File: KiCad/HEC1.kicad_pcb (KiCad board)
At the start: 2 copper layers, 243.8 x 170.2 mm, 36 parts, among them J1 Barrel_Jack_Switch, U1 Z80CPU, U10 74LS30, U11 74LS10, U11 74LS32, U12 74LS04, U13 74LS245, U14 74LS245, U15 74LS32, U16 74LS32, U17 74LS30, U17 74LS74, U18 74LS02, U18 74LS74, U19 74LS30, U2 AS6C4008-55PCN, U20 74LS574, U21 74LS574, U22 74LS02, U23 74LS74, U24 74LS74, U25 74LS541, U26 74LS541, U27 74LS74, U3 AS6C4008-55PCN, U4 CY7C199, U5 CY7C199, U6 74LS138, U7 28C256, U8 74LS138, U9 74LS574

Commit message: Add HEC Bus
The HEC bus packs a lot of information into a small amount of pins. It is suitable for cards with various complexity.
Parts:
- added REF**: edge_connector_8pin, Library:edge_connector_8pin, F.Cu at (66.0, 45.7)
- added REF**: edge_connector_36pin, Library:edge_connector_36pin, F.Cu at (66.0, 81.3)
- added REF**: edge_connector_8pin, Library:edge_connector_8pin, F.Cu at (124.5, 45.7)
- added REF**: edge_connector_36pin, Library:edge_connector_36pin, F.Cu at (154.9, 81.3)
- added REF**: edge_connector_36pin, Library:edge_connector_36pin, F.Cu at (96.5, 81.3)
- added REF**: edge_connector_8pin, Library:edge_connector_8pin, F.Cu at (96.5, 45.7)
- added REF**: edge_connector_8pin, Library:edge_connector_8pin, F.Cu at (154.9, 45.7)
- added REF**: edge_connector_36pin, Library:edge_connector_36pin, F.Cu at (124.5, 81.3)
- moved U11 317.2 mm to (428.9, 50.8)
- moved U11 317.2 mm to (413.7, -2.54)
- moved U12 317.2 mm to (440.7, 50.8)
- moved U15 317.2 mm to (368.3, 22.9)
- moved U16 317.2 mm to (380.1, 22.9)
- moved U20 317.2 mm to (403.4, 50.8)
- moved U21 317.2 mm to (415.2, 50.8)
- moved U22 317.2 mm to (425.4, -2.54)
- moved U6 317.2 mm to (413.7, 17.0)
- moved U6 317.2 mm to (428.9, 72.3)
- moved U7 317.2 mm to (384.0, 50.8)
- moved U8 317.2 mm to (425.4, 17.0)
- moved U9 317.2 mm to (393.4, 17.9)
- moved U10 283.6 mm to (325.1, 78.7)
- moved U1 188.0 mm to (332.7, 127.0)
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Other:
- outline, holes or cut-outs redrawn

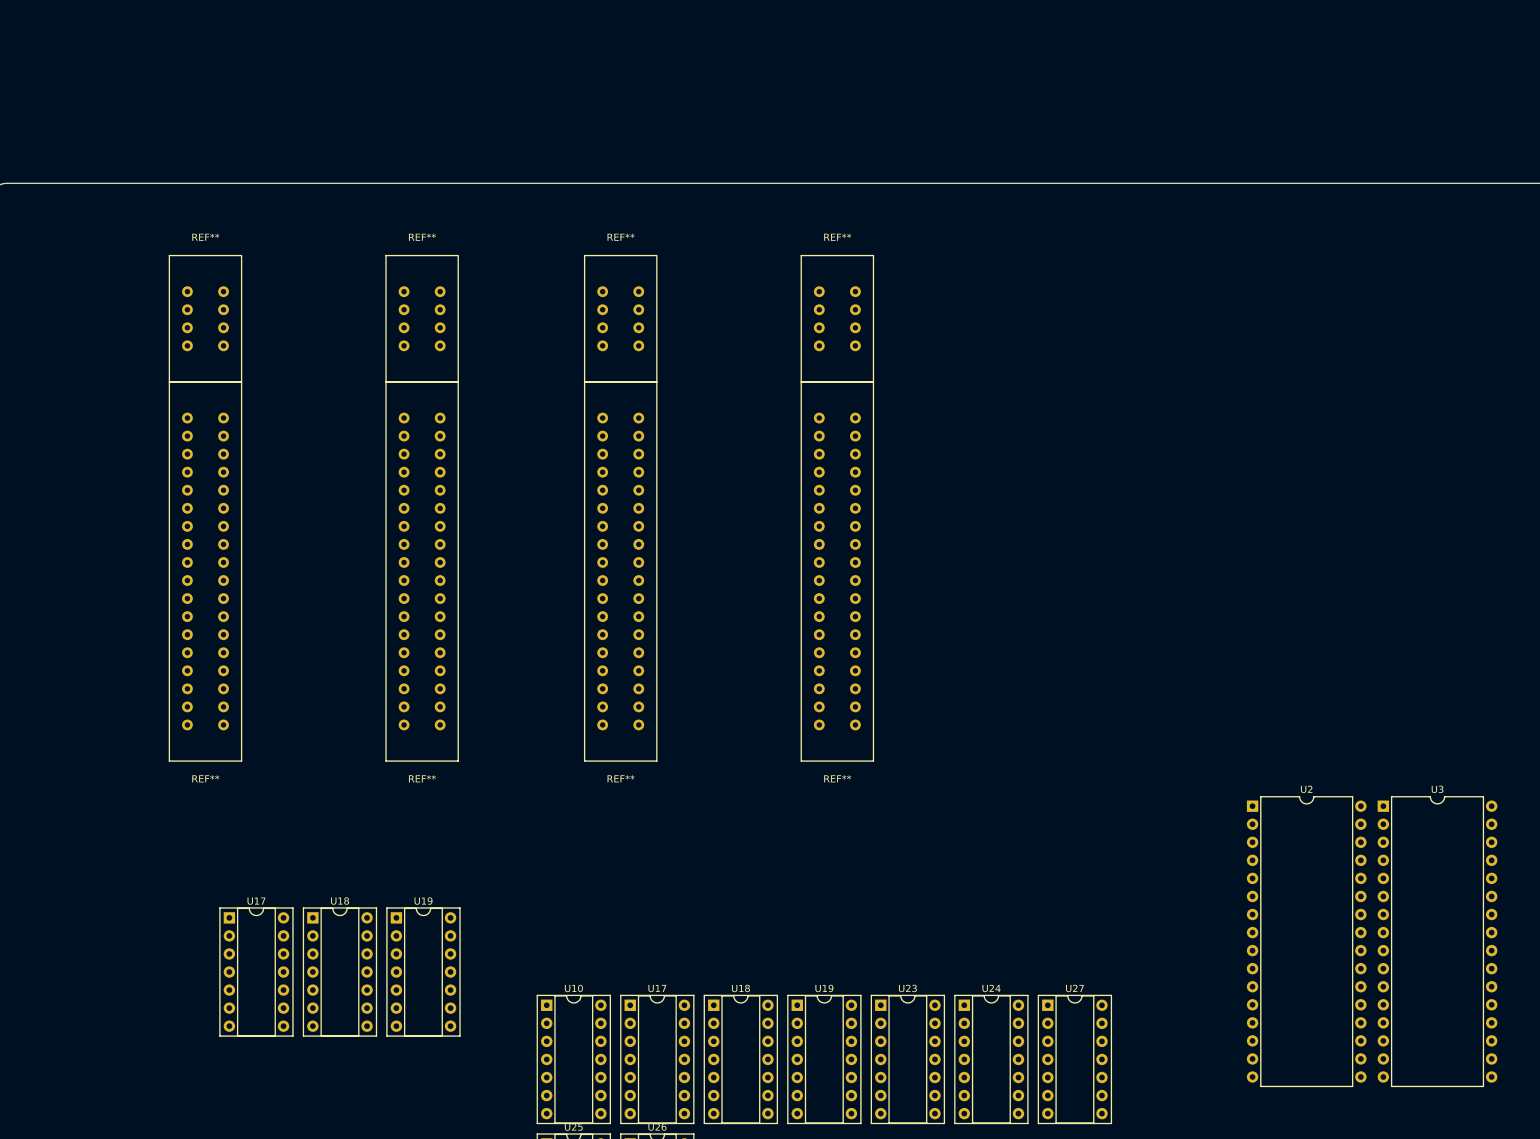
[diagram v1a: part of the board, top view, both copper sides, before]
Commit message: Created footprint for HEC bus
Created footprints for HEC bus and some other updates.
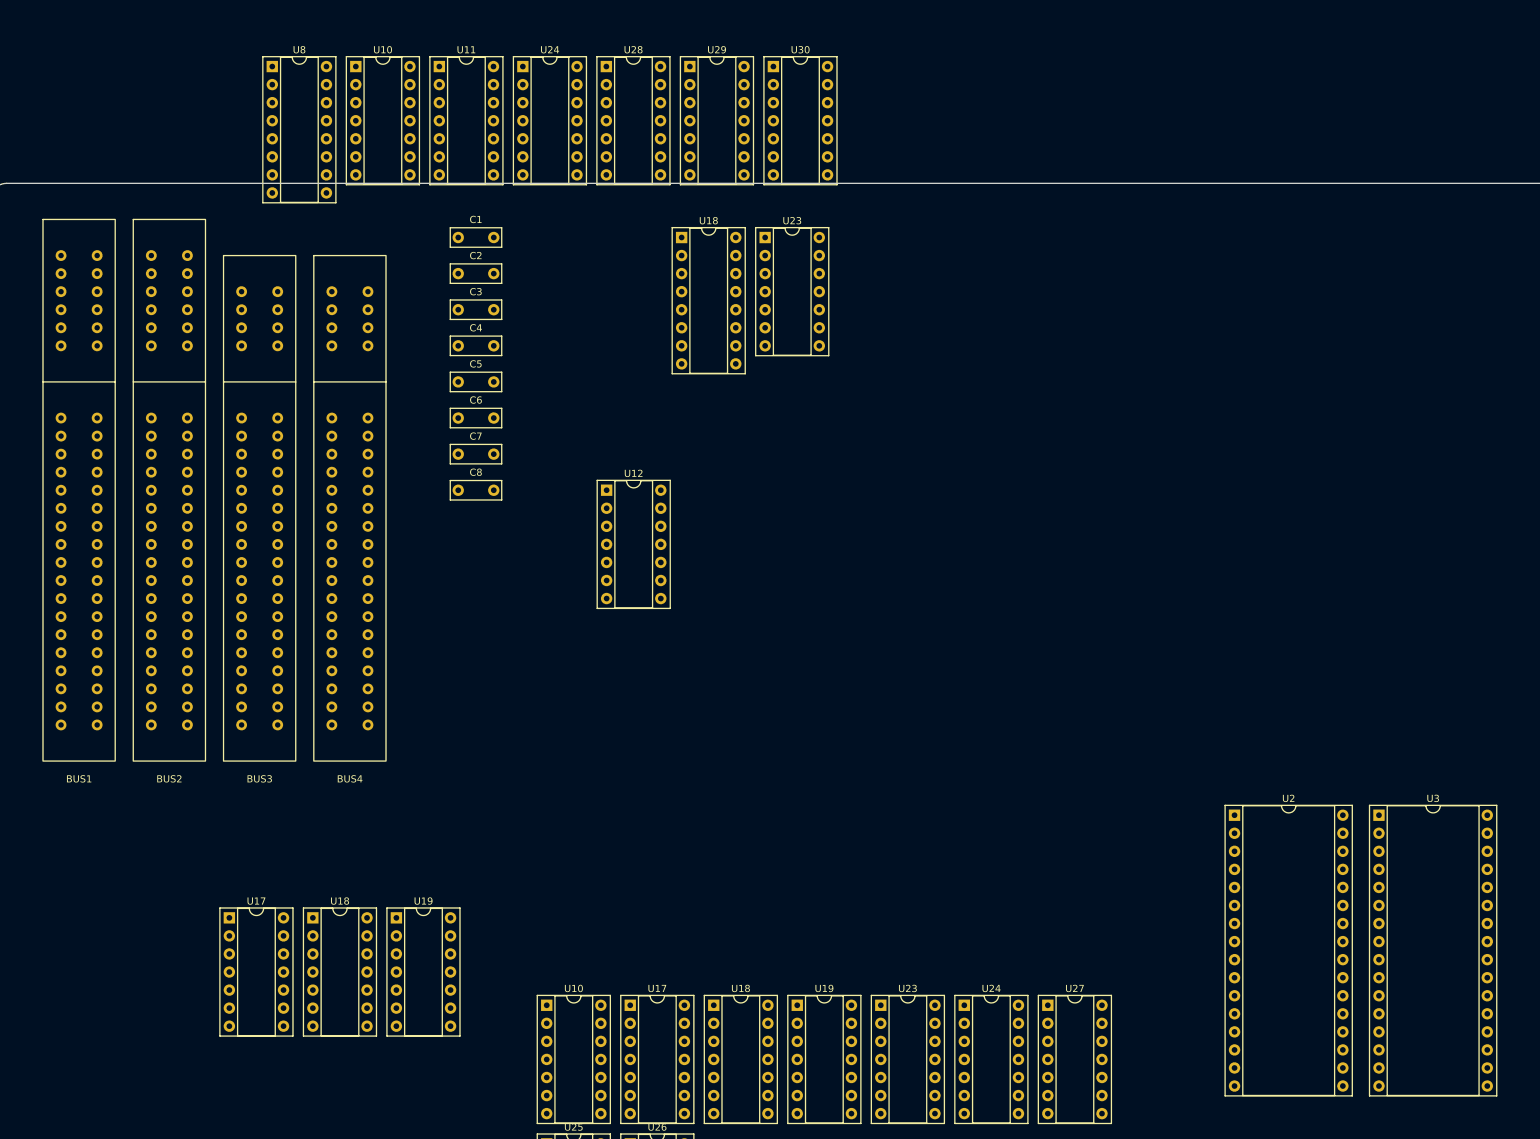
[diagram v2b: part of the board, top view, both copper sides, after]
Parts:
- removed REF** (x4): edge_connector_8pin, Library:edge_connector_8pin
- removed REF** (x4): edge_connector_36pin, Library:edge_connector_36pin
- added BUS1: ~, Library:Bus_HEC, F.Cu at (48.3, 68.6)
- added BUS2: ~, Library:Bus_HEC, F.Cu at (61.0, 68.6)
- added BUS3: ~, Library:Bus_HEC_5Vonly, F.Cu at (73.7, 68.6)
- added BUS4: ~, Library:Bus_HEC_5Vonly, F.Cu at (86.4, 68.6)
- added C1: C, Capacitor_THT:C_Disc_D7.0mm_W2.5mm_P5.00mm, F.Cu at (101.6, 33.0)
- added C2: C, Capacitor_THT:C_Disc_D7.0mm_W2.5mm_P5.00mm, F.Cu at (101.6, 38.1)
- added C3: C, Capacitor_THT:C_Disc_D7.0mm_W2.5mm_P5.00mm, F.Cu at (101.6, 43.2)
- added C4: C, Capacitor_THT:C_Disc_D7.0mm_W2.5mm_P5.00mm, F.Cu at (101.6, 48.3)
- added C5: C, Capacitor_THT:C_Disc_D7.0mm_W2.5mm_P5.00mm, F.Cu at (101.6, 53.3)
- added C6: C, Capacitor_THT:C_Disc_D7.0mm_W2.5mm_P5.00mm, F.Cu at (101.6, 58.4)
- added C7: C, Capacitor_THT:C_Disc_D7.0mm_W2.5mm_P5.00mm, F.Cu at (101.6, 63.5)
- added C8: C, Capacitor_THT:C_Disc_D7.0mm_W2.5mm_P5.00mm, F.Cu at (101.6, 68.6)
- added U10: 74LS32, Package_DIP:DIP-14_W7.62mm_Socket, F.Cu at (87.2, 8.97)
- added U11: 74LS00, Package_DIP:DIP-14_W7.62mm_Socket, F.Cu at (98.9, 8.97)
- added U12: 74LS04, Package_DIP:DIP-14_W7.62mm_Socket, F.Cu at (122.5, 68.6)
- added U18: 74LS138, Package_DIP:DIP-16_W7.62mm_Socket, F.Cu at (133.0, 33.0)
- added U23: 74LS74, Package_DIP:DIP-14_W7.62mm_Socket, F.Cu at (144.8, 33.0)
- added U24: 74LS74, Package_DIP:DIP-14_W7.62mm_Socket, F.Cu at (110.7, 8.97)
- added U28: 74LS20, Package_DIP:DIP-14_W7.62mm_Socket, F.Cu at (122.4, 8.97)
- added U29: 74LS74, Package_DIP:DIP-14_W7.62mm_Socket, F.Cu at (134.2, 8.97)
- added U30: 74LS74, Package_DIP:DIP-14_W7.62mm_Socket, F.Cu at (145.9, 8.97)
- added U8: 74LS138, Package_DIP:DIP-16_W7.62mm_Socket, F.Cu at (75.4, 8.97)
- U2, U3: footprint Package_DIP:DIP-32_W15.24mm -> Package_DIP:DIP-32_W15.24mm_Socket
- moved U2 2.84 mm to (210.8, 114.3)
- moved U3 1.41 mm to (231.1, 114.3)
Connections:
- J1 pad 1: unconnected-(J1-Pad1) -> VCC
- J1 pad 2: Net-(J1-Pad2) -> GND
- J1 pad 3: Net-(J1-Pad2) -> GND
- RN1 pad 1: /MEC_Protection/H -> H
- U1 pad 1: /HEC_CPU/A11 -> /HEC_Memory/A11
- U1 pad 10: /HEC_CPU/D6 -> /HEC_Memory/D6
- U1 pad 12: /HEC_CPU/D2 -> /HEC_Memory/D2
- U1 pad 13: /HEC_CPU/D7 -> /HEC_Memory/D7
- U1 pad 14: /HEC_CPU/D0 -> /HEC_Memory/D0
- U1 pad 15: /HEC_CPU/D1 -> /HEC_Memory/D1
- U1 pad 2: /HEC_CPU/A12 -> /HEC_Memory/A12
- U1 pad 3: /HEC_CPU/A13 -> /HEC_Memory/A13
- U1 pad 30: /HEC_CPU/A0 -> /HEC_Memory/A0
- U1 pad 31: /HEC_CPU/A1 -> /HEC_Memory/A1
- U1 pad 32: /HEC_CPU/A2 -> /HEC_Memory/A2
- U1 pad 33: /HEC_CPU/A3 -> /HEC_Memory/A3
- U1 pad 34: /HEC_CPU/A4 -> /HEC_Memory/A4
- U1 pad 35: /HEC_CPU/A5 -> /HEC_Memory/A5
- U1 pad 36: /HEC_CPU/A6 -> /HEC_Memory/A6
- U1 pad 37: /HEC_CPU/A7 -> /HEC_Memory/A7
- U1 pad 38: /HEC_CPU/A8 -> /HEC_Memory/A8
- U1 pad 39: /HEC_CPU/A9 -> /HEC_Memory/A9
- U1 pad 4: /HEC_CPU/A14 -> /HEC_Memory/A14
- U1 pad 40: /HEC_CPU/A10 -> /HEC_Memory/A10
- U1 pad 5: /HEC_CPU/A15 -> /HEC_Memory/A15
- U1 pad 7: /HEC_CPU/D4 -> /HEC_Memory/D4
- U1 pad 8: /HEC_CPU/D3 -> /HEC_Memory/D3
- U1 pad 9: /HEC_CPU/D5 -> /HEC_Memory/D5
- U17 pad 14: unconnected-(U17B-VCC-Pad14) -> VCC
- U17 pad 7: unconnected-(U17B-GND-Pad7) -> GND
- U17 pad 8: Net-(U17-Pad8) -> Net-(U10-Pad12)
- U19 pad 1: /MEC_Protection/D0 -> /HEC_Memory/A0
- U19 pad 11: /MEC_Protection/H -> H
- U19 pad 12: /MEC_Protection/H -> H
- U19 pad 2: /MEC_Protection/D1 -> /HEC_Memory/A1
- U19 pad 3: /MEC_Protection/D2 -> /HEC_Memory/A2
- U19 pad 4: /MEC_Protection/D6 -> /HEC_Memory/A6
- U19 pad 5: /MEC_Protection/D7 -> /HEC_Memory/A7
- U20 pad 12: /HEC_CPU/D7 -> /HEC_Memory/D7
- U20 pad 13: /HEC_CPU/D6 -> /HEC_Memory/D6
- U20 pad 14: /HEC_CPU/D5 -> /HEC_Memory/D5
- U20 pad 15: /HEC_CPU/D4 -> /HEC_Memory/D4
- U20 pad 16: /HEC_CPU/D3 -> /HEC_Memory/D3
- U20 pad 17: /HEC_CPU/D2 -> /HEC_Memory/D2
- U20 pad 18: /HEC_CPU/D1 -> /HEC_Memory/D1
- U20 pad 19: /HEC_CPU/D0 -> /HEC_Memory/D0
- U20 pad 2: /HEC_CPU/A0 -> /HEC_Memory/A0
- U20 pad 3: /HEC_CPU/A1 -> /HEC_Memory/A1
- U20 pad 4: /HEC_CPU/A2 -> /HEC_Memory/A2
- U20 pad 5: /HEC_CPU/A3 -> /HEC_Memory/A3
- U20 pad 6: /HEC_CPU/A4 -> /HEC_Memory/A4
- U20 pad 7: /HEC_CPU/A5 -> /HEC_Memory/A5
- U20 pad 8: /HEC_CPU/A6 -> /HEC_Memory/A6
- U20 pad 9: /HEC_CPU/A7 -> /HEC_Memory/A7
- U21 pad 12: /HEC_CPU/D7 -> /HEC_Memory/D7
- U21 pad 13: /HEC_CPU/D6 -> /HEC_Memory/D6
- U21 pad 14: /HEC_CPU/D5 -> /HEC_Memory/D5
- U21 pad 15: /HEC_CPU/D4 -> /HEC_Memory/D4
- U21 pad 16: /HEC_CPU/D3 -> /HEC_Memory/D3
- U21 pad 17: /HEC_CPU/D2 -> /HEC_Memory/D2
- U21 pad 18: /HEC_CPU/D1 -> /HEC_Memory/D1
- U21 pad 19: /HEC_CPU/D0 -> /HEC_Memory/D0
- U21 pad 2: /HEC_CPU/A8 -> /HEC_Memory/A8
- U21 pad 3: /HEC_CPU/A9 -> /HEC_Memory/A9
- U21 pad 4: /HEC_CPU/A10 -> /HEC_Memory/A10
- U21 pad 5: /HEC_CPU/A11 -> /HEC_Memory/A11
- U21 pad 6: /HEC_CPU/A12 -> /HEC_Memory/A12
- U21 pad 7: /HEC_CPU/A13 -> /HEC_Memory/A13
- U21 pad 8: /HEC_CPU/A14 -> /HEC_Memory/A14
- U21 pad 9: /HEC_CPU/A15 -> /HEC_Memory/A15
- U22 pad 1: (no net) -> unconnected-(U22-Pad1)
- U22 pad 11: unconnected-(U22-Pad11) -> /MEC_Protection/SYS
- U22 pad 12: unconnected-(U22-Pad12) -> /MEC_Protection/~{IORQ}
- U22 pad 13: unconnected-(U22-Pad13) -> Net-(U30A-C)
- U22 pad 2: (no net) -> unconnected-(U22-Pad2)
- U22 pad 3: (no net) -> unconnected-(U22-Pad3)
- U25 pad 1: unconnected-(U25-G1-Pad1) -> /HEC_CPU/~{RD}
- U25 pad 10: unconnected-(U25-GND-Pad10) -> GND
- U25 pad 11: unconnected-(U25-Y7-Pad11) -> /HEC_Memory/A7
- U25 pad 12: unconnected-(U25-Y6-Pad12) -> /HEC_Memory/A6
- U25 pad 13: unconnected-(U25-Y5-Pad13) -> /HEC_Memory/A5
- U25 pad 14: unconnected-(U25-Y4-Pad14) -> /HEC_Memory/A4
- U25 pad 15: unconnected-(U25-Y3-Pad15) -> /HEC_Memory/A3
- U25 pad 16: unconnected-(U25-Y2-Pad16) -> /HEC_Memory/A2
- U25 pad 17: unconnected-(U25-Y1-Pad17) -> /HEC_Memory/A1
- U25 pad 18: unconnected-(U25-Y0-Pad18) -> /HEC_Memory/A0
- U25 pad 19: unconnected-(U25-G2-Pad19) -> /MEC_Protection/~{INT_SOURCE_1}
- U25 pad 20: unconnected-(U25-VCC-Pad20) -> VCC
- U26 pad 1: unconnected-(U26-G1-Pad1) -> /HEC_CPU/~{RD}
- U26 pad 10: unconnected-(U26-GND-Pad10) -> GND
- U26 pad 11: unconnected-(U26-Y7-Pad11) -> /HEC_Memory/A7
- U26 pad 12: unconnected-(U26-Y6-Pad12) -> /HEC_Memory/A6
- U26 pad 13: unconnected-(U26-Y5-Pad13) -> /HEC_Memory/A5
- U26 pad 14: unconnected-(U26-Y4-Pad14) -> /HEC_Memory/A4
- U26 pad 15: unconnected-(U26-Y3-Pad15) -> /HEC_Memory/A3
- U26 pad 16: unconnected-(U26-Y2-Pad16) -> /HEC_Memory/A2
- U26 pad 17: unconnected-(U26-Y1-Pad17) -> /HEC_Memory/A1
- U26 pad 18: unconnected-(U26-Y0-Pad18) -> /HEC_Memory/A0
- U26 pad 19: unconnected-(U26-G2-Pad19) -> /MEC_Protection/~{INT_SOURCE_2}
- U26 pad 2: /MEC_Protection/lastsys -> /MEC_Protection/~{EXT_INT0}
- U26 pad 20: unconnected-(U26-VCC-Pad20) -> VCC
- U27 pad 1: Net-(U23B-Q) -> /HEC_CPU/~{NMI}
- U27 pad 10: /MEC_Protection/H -> H
- U27 pad 13: /MEC_Protection/H -> H
- U6 pad 1: /HEC_CPU/A4 -> /HEC_Memory/A4
- U6 pad 2: /HEC_CPU/A5 -> /HEC_Memory/A5
- U6 pad 3: /HEC_CPU/A6 -> /HEC_Memory/A6
- U6 pad 4: /HEC_CPU/A7 -> /HEC_Memory/A7
- U7 pad 1: /HEC_CPU/A14 -> /HEC_Memory/A14
- U7 pad 10: /HEC_CPU/A0 -> /HEC_Memory/A0
- U7 pad 11: /HEC_CPU/D0 -> /HEC_Memory/D0
- U7 pad 12: /HEC_CPU/D1 -> /HEC_Memory/D1
- U7 pad 13: /HEC_CPU/D2 -> /HEC_Memory/D2
- U7 pad 15: /HEC_CPU/D3 -> /HEC_Memory/D3
- U7 pad 16: /HEC_CPU/D4 -> /HEC_Memory/D4
- U7 pad 17: /HEC_CPU/D5 -> /HEC_Memory/D5
- U7 pad 18: /HEC_CPU/D6 -> /HEC_Memory/D6
- U7 pad 19: /HEC_CPU/D7 -> /HEC_Memory/D7
- U7 pad 2: /HEC_CPU/A12 -> /HEC_Memory/A12
- U7 pad 20: unconnected-(U7-~{CS}-Pad20) -> /HEC_Memory/A15
- U7 pad 21: /HEC_CPU/A10 -> /HEC_Memory/A10
- U7 pad 22: unconnected-(U7-~{OE}-Pad22) -> /HEC_CPU/ROM
- U7 pad 23: /HEC_CPU/A11 -> /HEC_Memory/A11
- U7 pad 24: /HEC_CPU/A9 -> /HEC_Memory/A9
- U7 pad 25: /HEC_CPU/A8 -> /HEC_Memory/A8
- U7 pad 26: /HEC_CPU/A13 -> /HEC_Memory/A13
- U7 pad 27: unconnected-(U7-~{WE}-Pad27) -> /HEC_CPU/H
- U7 pad 3: /HEC_CPU/A7 -> /HEC_Memory/A7
- U7 pad 4: /HEC_CPU/A6 -> /HEC_Memory/A6
- U7 pad 5: /HEC_CPU/A5 -> /HEC_Memory/A5
- U7 pad 6: /HEC_CPU/A4 -> /HEC_Memory/A4
- U7 pad 7: /HEC_CPU/A3 -> /HEC_Memory/A3
- U7 pad 8: /HEC_CPU/A2 -> /HEC_Memory/A2
- U7 pad 9: /HEC_CPU/A1 -> /HEC_Memory/A1

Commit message: MATX-compliant motherboard
Made the motherboard mounting holes and card positions MATX compliant. The MATX motherboard edge is shifted 0.5 inches to the left, which is annoying. Also, cards have component on the opposite side from ISA, meaning PCI slot positioning must be followed. However, PCI pins are not 0.1inch apart, so lining up is tricky. I don't know whether I got it right.
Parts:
- added H1: MountingHole_Pad, MountingHole:MountingHole_3.2mm_M3_Pad_Via, F.Cu at (68.6, 35.6)
- added H2: MountingHole_Pad, MountingHole:MountingHole_3.2mm_M3_Pad_Via, F.Cu at (271.8, 58.4)
- added H3: MountingHole_Pad, MountingHole:MountingHole_3.2mm_M3_Pad_Via, F.Cu at (114.3, 190.5)
- added H4: MountingHole_Pad, MountingHole:MountingHole_3.2mm_M3_Pad_Via, F.Cu at (193.0, 18.8)
- added H5: MountingHole_Pad, MountingHole:MountingHole_3.2mm_M3_Pad_Via, F.Cu at (114.3, 35.6)
- added H6: MountingHole_Pad, MountingHole:MountingHole_3.2mm_M3_Pad_Via, F.Cu at (271.8, 190.5)
- added H7: MountingHole_Pad, MountingHole:MountingHole_3.2mm_M3_Pad_Via, F.Cu at (48.3, 190.5)
- added J2: Conn_02x03_Odd_Even, Connector_PinHeader_2.54mm:PinHeader_2x03_P2.54mm_Vertical, F.Cu at (223.4, -43.8)
- added J3: Conn_02x05_Odd_Even, Connector_PinHeader_2.54mm:PinHeader_2x05_P2.54mm_Vertical, F.Cu at (221.0, -6.70)
- added J4: Conn_02x13_Odd_Even, Connector_PinHeader_2.54mm:PinHeader_2x13_P2.54mm_Vertical, F.Cu at (191.4, -43.8)
- added PS1: ITX0512S, Converter_DCDC:Converter_DCDC_XP_POWER-ITxxxxxS_THT, F.Cu at (132.1, 53.3)
- added RN1: R_Network08, Resistor_THT:R_Array_SIP9, F.Cu at (198.5, -44.0)
- added RN2: R_Network08, Resistor_THT:R_Array_SIP9, F.Cu at (198.5, -39.6)
- added U12: 74LS04, Package_DIP:DIP-14_W7.62mm_Socket, F.Cu at (191.1, -63.5)
- added U17: 74LS20, Package_DIP:DIP-14_W7.62mm_Socket, F.Cu at (202.9, -63.5)
- added U22: 74LS02, Package_DIP:DIP-14_W7.62mm_Socket, F.Cu at (237.0, -6.90)
- added U30: 74LS74, Package_DIP:DIP-14_W7.62mm_Socket, F.Cu at (214.6, -63.5)
- added U31: 74LS32, Package_DIP:DIP-14_W7.62mm_Socket, F.Cu at (226.4, -63.5)
- added U32: LM79M05_TO220, Package_TO_SOT_THT:TO-92_Inline, F.Cu at (223.0, -33.2)
- added U33: 74LS20, Package_DIP:DIP-14_W7.62mm_Socket, F.Cu at (238.1, -63.5)
- added U34: 74LS393, Package_DIP:DIP-14_W7.62mm_Socket, F.Cu at (209.0, -6.90)
- added U35: 74LS08, Package_DIP:DIP-14_W7.62mm_Socket, F.Cu at (249.9, -63.5)
- added U36: 74LS27, Package_DIP:DIP-14_W7.62mm_Socket, F.Cu at (261.6, -63.5)
- added U6: 74LS138, Package_DIP:DIP-16_W7.62mm_Socket, F.Cu at (209.6, -35.3)
- added X1: CXO_DIP8, Oscillator:Oscillator_DIP-8, F.Cu at (222.0, 16.7)
- moved RN1 345.9 mm to (392.9, -50.0)
- moved U17 345.9 mm to (325.1, -104.1)
- moved U18 345.9 mm to (336.9, -104.1)
- moved U19 345.9 mm to (348.6, -104.1)
- moved U2 345.9 mm to (466.5, -118.6)
- moved U3 345.9 mm to (486.9, -118.6)
- moved U10 345.9 mm to (369.8, -91.8)
- moved U17 345.9 mm to (381.5, -91.8)
- moved U18 345.9 mm to (393.3, -91.8)
- moved U19 345.9 mm to (405.0, -91.8)
- moved U23 345.9 mm to (416.8, -91.8)
- moved U24 345.9 mm to (428.5, -91.8)
- moved U25 345.9 mm to (369.8, -72.3)
- moved U26 345.9 mm to (381.5, -72.3)
- moved U27 345.9 mm to (440.3, -91.8)
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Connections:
- net /MEC_Protection/IO_CS0 renamed /MEC_Protection/~{IO_CS0}
- BUS1 pad 1: unconnected-(BUS1-A0-Pad1) -> /HEC_IO/A8
- BUS1 pad 10: unconnected-(BUS1-D4-Pad10) -> /HEC_IO/D4
- BUS1 pad 11: unconnected-(BUS1-A5-Pad11) -> /HEC_IO/A13
- BUS1 pad 12: unconnected-(BUS1-D5-Pad12) -> /HEC_IO/D5
- BUS1 pad 13: unconnected-(BUS1-A6-Pad13) -> /HEC_IO/A14
- BUS1 pad 14: unconnected-(BUS1-D6-Pad14) -> /HEC_IO/D6
- BUS1 pad 15: unconnected-(BUS1-A7-Pad15) -> /HEC_IO/A15
- BUS1 pad 16: unconnected-(BUS1-D7-Pad16) -> /HEC_IO/D7
- BUS1 pad 17: unconnected-(BUS1-~{DACK}-Pad17) -> H
- BUS1 pad 18: unconnected-(BUS1-~{CS}-Pad18) -> /HEC_IO/~{IO_CS2}
- BUS1 pad 2: unconnected-(BUS1-D0-Pad2) -> /HEC_IO/D0
- BUS1 pad 20: unconnected-(BUS1-~{RD}-Pad20) -> /HEC_IO/~{RD}
- BUS1 pad 21: unconnected-(BUS1-~{ROMWR}-Pad21) -> H
- BUS1 pad 22: unconnected-(BUS1-~{WR}-Pad22) -> /HEC_CPU/~{WR}
- BUS1 pad 24: unconnected-(BUS1-PA0-Pad24) -> /HEC_IO/A0
- BUS1 pad 25: unconnected-(BUS1-~{IRQ}-Pad25) -> /HEC_IO/~{IRQ1}
- BUS1 pad 26: unconnected-(BUS1-PA1-Pad26) -> /HEC_IO/A1
- BUS1 pad 27: unconnected-(BUS1-~{RESET}-Pad27) -> /HEC_IO/~{RESET}
- BUS1 pad 28: unconnected-(BUS1-PA2-Pad28) -> /HEC_IO/A2
- BUS1 pad 29: unconnected-(BUS1-CLK-Pad29) -> /HEC_IO/OSC
- BUS1 pad 3: unconnected-(BUS1-A1-Pad3) -> /HEC_IO/A9
- BUS1 pad 30: unconnected-(BUS1-PA3-Pad30) -> /HEC_IO/A3
- BUS1 pad 31: unconnected-(BUS1-~{WAIT}-Pad31) -> /HEC_IO/~{WAIT1}
- BUS1 pad 32: unconnected-(BUS1-PA4-Pad32) -> /HEC_IO/A4
- BUS1 pad 33: unconnected-(BUS1-~{NOWS}-Pad33) -> /HEC_IO/~{NOWS1}
- BUS1 pad 34: unconnected-(BUS1-~{SENSE}-Pad34) -> /HEC_IO/~{SENSE1}
- BUS1 pad 35: unconnected-(BUS1-GND-Pad35) -> L
- BUS1 pad 36: unconnected-(BUS1-GND-Pad36) -> L
- BUS1 pad 4: unconnected-(BUS1-D1-Pad4) -> /HEC_IO/D1
- BUS1 pad 5: unconnected-(BUS1-A2-Pad5) -> /HEC_IO/A10
- BUS1 pad 6: unconnected-(BUS1-D2-Pad6) -> /HEC_IO/D2
- BUS1 pad 7: unconnected-(BUS1-A3-Pad7) -> /HEC_IO/A11
- BUS1 pad 8: unconnected-(BUS1-D3-Pad8) -> /HEC_IO/D3
- BUS1 pad 9: unconnected-(BUS1-A4-Pad9) -> /HEC_IO/A12
- BUS1 pad P1: unconnected-(BUS1--5V-PadP1) -> /HEC_IO/-5V
- BUS1 pad P10: unconnected-(BUS1-+5V-PadP10) -> H
- BUS1 pad P11: unconnected-(BUS1-+5V-PadP11) -> H
- BUS1 pad P12: unconnected-(BUS1-+5V-PadP12) -> H
- BUS1 pad P2: unconnected-(BUS1--12V-PadP2) -> /HEC_IO/-12V
- BUS1 pad P3: unconnected-(BUS1-GND-PadP3) -> L
- BUS1 pad P4: unconnected-(BUS1-+12V-PadP4) -> /HEC_IO/+12V
- BUS1 pad P5: unconnected-(BUS1-GND-PadP5) -> L
- BUS1 pad P6: unconnected-(BUS1-GND-PadP6) -> L
- BUS1 pad P7: unconnected-(BUS1-GND-PadP7) -> L
- BUS1 pad P8: unconnected-(BUS1-GND-PadP8) -> L
- BUS1 pad P9: unconnected-(BUS1-+5V-PadP9) -> H
- BUS2 pad 1: unconnected-(BUS2-A0-Pad1) -> /HEC_IO/A8
- BUS2 pad 10: unconnected-(BUS2-D4-Pad10) -> /HEC_IO/D4
- BUS2 pad 11: unconnected-(BUS2-A5-Pad11) -> /HEC_IO/A13
- BUS2 pad 12: unconnected-(BUS2-D5-Pad12) -> /HEC_IO/D5
- BUS2 pad 13: unconnected-(BUS2-A6-Pad13) -> /HEC_IO/A14
- BUS2 pad 14: unconnected-(BUS2-D6-Pad14) -> /HEC_IO/D6
- BUS2 pad 15: unconnected-(BUS2-A7-Pad15) -> /HEC_IO/A15
- BUS2 pad 16: unconnected-(BUS2-D7-Pad16) -> /HEC_IO/D7
- BUS2 pad 17: unconnected-(BUS2-~{DACK}-Pad17) -> H
- BUS2 pad 18: unconnected-(BUS2-~{CS}-Pad18) -> /HEC_IO/~{IO_CS3}
- BUS2 pad 2: unconnected-(BUS2-D0-Pad2) -> /HEC_IO/D0
- BUS2 pad 20: unconnected-(BUS2-~{RD}-Pad20) -> /HEC_IO/~{RD}
- BUS2 pad 21: unconnected-(BUS2-~{ROMWR}-Pad21) -> H
- BUS2 pad 22: unconnected-(BUS2-~{WR}-Pad22) -> /HEC_CPU/~{WR}
- BUS2 pad 24: unconnected-(BUS2-PA0-Pad24) -> /HEC_IO/A0
- BUS2 pad 25: unconnected-(BUS2-~{IRQ}-Pad25) -> /HEC_IO/~{IRQ2}
- BUS2 pad 26: unconnected-(BUS2-PA1-Pad26) -> /HEC_IO/A1
- BUS2 pad 27: unconnected-(BUS2-~{RESET}-Pad27) -> /HEC_IO/~{RESET}
- BUS2 pad 28: unconnected-(BUS2-PA2-Pad28) -> /HEC_IO/A2
- BUS2 pad 29: unconnected-(BUS2-CLK-Pad29) -> /HEC_IO/OSC
- BUS2 pad 3: unconnected-(BUS2-A1-Pad3) -> /HEC_IO/A9
- BUS2 pad 30: unconnected-(BUS2-PA3-Pad30) -> /HEC_IO/A3
- BUS2 pad 31: unconnected-(BUS2-~{WAIT}-Pad31) -> /HEC_IO/~{WAIT2}
- BUS2 pad 32: unconnected-(BUS2-PA4-Pad32) -> /HEC_IO/A4
- BUS2 pad 33: unconnected-(BUS2-~{NOWS}-Pad33) -> /HEC_IO/~{NOWS2}
- BUS2 pad 34: unconnected-(BUS2-~{SENSE}-Pad34) -> /HEC_IO/~{SENSE2}
- BUS2 pad 35: unconnected-(BUS2-GND-Pad35) -> L
- BUS2 pad 36: unconnected-(BUS2-GND-Pad36) -> L
- BUS2 pad 4: unconnected-(BUS2-D1-Pad4) -> /HEC_IO/D1
- BUS2 pad 5: unconnected-(BUS2-A2-Pad5) -> /HEC_IO/A10
- BUS2 pad 6: unconnected-(BUS2-D2-Pad6) -> /HEC_IO/D2
- BUS2 pad 7: unconnected-(BUS2-A3-Pad7) -> /HEC_IO/A11
- BUS2 pad 8: unconnected-(BUS2-D3-Pad8) -> /HEC_IO/D3
- BUS2 pad 9: unconnected-(BUS2-A4-Pad9) -> /HEC_IO/A12
- BUS2 pad P1: unconnected-(BUS2--5V-PadP1) -> /HEC_IO/-5V
- BUS2 pad P10: unconnected-(BUS2-+5V-PadP10) -> H
- BUS2 pad P11: unconnected-(BUS2-+5V-PadP11) -> H
- BUS2 pad P12: unconnected-(BUS2-+5V-PadP12) -> H
- BUS2 pad P2: unconnected-(BUS2--12V-PadP2) -> /HEC_IO/-12V
- BUS2 pad P3: unconnected-(BUS2-GND-PadP3) -> L
- BUS2 pad P4: unconnected-(BUS2-+12V-PadP4) -> /HEC_IO/+12V
- BUS2 pad P5: unconnected-(BUS2-GND-PadP5) -> L
- BUS2 pad P6: unconnected-(BUS2-GND-PadP6) -> L
- BUS2 pad P7: unconnected-(BUS2-GND-PadP7) -> L
- BUS2 pad P8: unconnected-(BUS2-GND-PadP8) -> L
- BUS2 pad P9: unconnected-(BUS2-+5V-PadP9) -> H
- BUS3 pad 1: unconnected-(BUS3-A0-Pad1) -> /HEC_IO/A8
- BUS3 pad 10: unconnected-(BUS3-D4-Pad10) -> /HEC_IO/D4
- BUS3 pad 11: unconnected-(BUS3-A5-Pad11) -> /HEC_IO/A13
- BUS3 pad 12: unconnected-(BUS3-D5-Pad12) -> /HEC_IO/D5
- BUS3 pad 13: unconnected-(BUS3-A6-Pad13) -> /HEC_IO/A14
- BUS3 pad 14: unconnected-(BUS3-D6-Pad14) -> /HEC_IO/D6
- BUS3 pad 15: unconnected-(BUS3-A7-Pad15) -> /HEC_IO/A15
- BUS3 pad 16: unconnected-(BUS3-D7-Pad16) -> /HEC_IO/D7
- BUS3 pad 17: unconnected-(BUS3-~{DACK}-Pad17) -> H
- BUS3 pad 18: unconnected-(BUS3-~{CS}-Pad18) -> /HEC_IO/~{IO_CS4}
- BUS3 pad 2: unconnected-(BUS3-D0-Pad2) -> /HEC_IO/D0
- BUS3 pad 20: unconnected-(BUS3-~{RD}-Pad20) -> /HEC_IO/~{RD}
- BUS3 pad 21: unconnected-(BUS3-~{ROMWR}-Pad21) -> H
- BUS3 pad 22: unconnected-(BUS3-~{WR}-Pad22) -> /HEC_CPU/~{WR}
- BUS3 pad 24: unconnected-(BUS3-PA0-Pad24) -> /HEC_IO/A0
- BUS3 pad 25: unconnected-(BUS3-~{IRQ}-Pad25) -> /HEC_IO/~{IRQ3}
- BUS3 pad 26: unconnected-(BUS3-PA1-Pad26) -> /HEC_IO/A1
- BUS3 pad 27: unconnected-(BUS3-~{RESET}-Pad27) -> /HEC_IO/~{RESET}
- BUS3 pad 28: unconnected-(BUS3-PA2-Pad28) -> /HEC_IO/A2
- BUS3 pad 29: unconnected-(BUS3-CLK-Pad29) -> /HEC_IO/OSC
- BUS3 pad 3: unconnected-(BUS3-A1-Pad3) -> /HEC_IO/A9
- BUS3 pad 30: unconnected-(BUS3-PA3-Pad30) -> /HEC_IO/A3
- BUS3 pad 31: unconnected-(BUS3-~{WAIT}-Pad31) -> /HEC_IO/~{WAIT3}
- BUS3 pad 32: unconnected-(BUS3-PA4-Pad32) -> /HEC_IO/A4
- BUS3 pad 33: unconnected-(BUS3-~{NOWS}-Pad33) -> /HEC_IO/~{NOWS3}
- BUS3 pad 34: unconnected-(BUS3-~{SENSE}-Pad34) -> /HEC_IO/~{SENSE3}
- BUS3 pad 35: unconnected-(BUS3-GND-Pad35) -> L
- BUS3 pad 36: unconnected-(BUS3-GND-Pad36) -> L
- BUS3 pad 4: unconnected-(BUS3-D1-Pad4) -> /HEC_IO/D1
- BUS3 pad 5: unconnected-(BUS3-A2-Pad5) -> /HEC_IO/A10
- BUS3 pad 6: unconnected-(BUS3-D2-Pad6) -> /HEC_IO/D2
- BUS3 pad 7: unconnected-(BUS3-A3-Pad7) -> /HEC_IO/A11
- BUS3 pad 8: unconnected-(BUS3-D3-Pad8) -> /HEC_IO/D3
- BUS3 pad 9: unconnected-(BUS3-A4-Pad9) -> /HEC_IO/A12
- BUS3 pad P10: unconnected-(BUS3-+5V-PadP10) -> H
- BUS3 pad P11: unconnected-(BUS3-+5V-PadP11) -> H
- BUS3 pad P12: unconnected-(BUS3-+5V-PadP12) -> H
- BUS3 pad P5: unconnected-(BUS3-GND-PadP5) -> L
- BUS3 pad P6: unconnected-(BUS3-GND-PadP6) -> L
- BUS3 pad P7: unconnected-(BUS3-GND-PadP7) -> L
- BUS3 pad P8: unconnected-(BUS3-GND-PadP8) -> L
- BUS3 pad P9: unconnected-(BUS3-+5V-PadP9) -> H
- BUS4 pad 1: unconnected-(BUS4-A0-Pad1) -> /HEC_IO/A8
- BUS4 pad 10: unconnected-(BUS4-D4-Pad10) -> /HEC_IO/D4
- BUS4 pad 11: unconnected-(BUS4-A5-Pad11) -> /HEC_IO/A13
- BUS4 pad 12: unconnected-(BUS4-D5-Pad12) -> /HEC_IO/D5
- BUS4 pad 13: unconnected-(BUS4-A6-Pad13) -> /HEC_IO/A14
- BUS4 pad 14: unconnected-(BUS4-D6-Pad14) -> /HEC_IO/D6
- BUS4 pad 15: unconnected-(BUS4-A7-Pad15) -> /HEC_IO/A15
- BUS4 pad 16: unconnected-(BUS4-D7-Pad16) -> /HEC_IO/D7
- BUS4 pad 17: unconnected-(BUS4-~{DACK}-Pad17) -> H
- BUS4 pad 18: unconnected-(BUS4-~{CS}-Pad18) -> Net-(BUS4-~{CS})
- BUS4 pad 2: unconnected-(BUS4-D0-Pad2) -> /HEC_IO/D0
- BUS4 pad 20: unconnected-(BUS4-~{RD}-Pad20) -> /HEC_IO/~{RD}
- BUS4 pad 21: unconnected-(BUS4-~{ROMWR}-Pad21) -> H
- BUS4 pad 22: unconnected-(BUS4-~{WR}-Pad22) -> /HEC_CPU/~{WR}
- BUS4 pad 24: unconnected-(BUS4-PA0-Pad24) -> /HEC_IO/A0
- BUS4 pad 25: unconnected-(BUS4-~{IRQ}-Pad25) -> /HEC_IO/~{IRQ4}
- BUS4 pad 26: unconnected-(BUS4-PA1-Pad26) -> /HEC_IO/A1
- BUS4 pad 27: unconnected-(BUS4-~{RESET}-Pad27) -> /HEC_IO/~{RESET}
- BUS4 pad 28: unconnected-(BUS4-PA2-Pad28) -> /HEC_IO/A2
- BUS4 pad 29: unconnected-(BUS4-CLK-Pad29) -> /HEC_IO/OSC
- BUS4 pad 3: unconnected-(BUS4-A1-Pad3) -> /HEC_IO/A9
- BUS4 pad 30: unconnected-(BUS4-PA3-Pad30) -> /HEC_IO/A3
- BUS4 pad 31: unconnected-(BUS4-~{WAIT}-Pad31) -> /HEC_IO/~{WAIT4}
- BUS4 pad 32: unconnected-(BUS4-PA4-Pad32) -> /HEC_IO/A4
- BUS4 pad 33: unconnected-(BUS4-~{NOWS}-Pad33) -> /HEC_IO/~{NOWS4}
- BUS4 pad 34: unconnected-(BUS4-~{SENSE}-Pad34) -> /HEC_IO/~{SENSE4}
- BUS4 pad 35: unconnected-(BUS4-GND-Pad35) -> L
- BUS4 pad 36: unconnected-(BUS4-GND-Pad36) -> L
- BUS4 pad 4: unconnected-(BUS4-D1-Pad4) -> /HEC_IO/D1
- BUS4 pad 5: unconnected-(BUS4-A2-Pad5) -> /HEC_IO/A10
- BUS4 pad 6: unconnected-(BUS4-D2-Pad6) -> /HEC_IO/D2
- BUS4 pad 7: unconnected-(BUS4-A3-Pad7) -> /HEC_IO/A11
- BUS4 pad 8: unconnected-(BUS4-D3-Pad8) -> /HEC_IO/D3
- BUS4 pad 9: unconnected-(BUS4-A4-Pad9) -> /HEC_IO/A12
- BUS4 pad P10: unconnected-(BUS4-+5V-PadP10) -> H
- BUS4 pad P11: unconnected-(BUS4-+5V-PadP11) -> H
- BUS4 pad P12: unconnected-(BUS4-+5V-PadP12) -> H
- BUS4 pad P5: unconnected-(BUS4-GND-PadP5) -> L
- BUS4 pad P6: unconnected-(BUS4-GND-PadP6) -> L
- BUS4 pad P7: unconnected-(BUS4-GND-PadP7) -> L
- BUS4 pad P8: unconnected-(BUS4-GND-PadP8) -> L
- BUS4 pad P9: unconnected-(BUS4-+5V-PadP9) -> H
- C1 pad 1: VCC -> H
- C1 pad 2: GND -> L
- C2 pad 1: VCC -> H
- C2 pad 2: GND -> L
- C3 pad 1: VCC -> H
- C3 pad 2: GND -> L
- C4 pad 1: VCC -> H
- C4 pad 2: GND -> L
- C5 pad 1: VCC -> H
- C5 pad 2: GND -> L
- C6 pad 1: VCC -> H
- C6 pad 2: GND -> L
- C7 pad 1: VCC -> H
- C7 pad 2: GND -> L
- C8 pad 1: VCC -> H
- C8 pad 2: GND -> L
- J1 pad 1: VCC -> H
- J1 pad 2: GND -> L
- J1 pad 3: GND -> L
- U1 pad 1: /HEC_Memory/A11 -> /HEC_IO/A11
- U1 pad 11: VCC -> H
- U1 pad 16: /HEC_CPU/H -> H
- U1 pad 2: /HEC_Memory/A12 -> /HEC_IO/A12
- U1 pad 25: /HEC_CPU/H -> H
- U1 pad 27: /HEC_CPU/~{M1} -> /MEC_Protection/~{M1}
- U1 pad 29: GND -> L
- U1 pad 3: /HEC_Memory/A13 -> /HEC_IO/A13
- U1 pad 30: /HEC_Memory/A0 -> /HEC_IO/A0
- U1 pad 31: /HEC_Memory/A1 -> /HEC_IO/A1
- U1 pad 32: /HEC_Memory/A2 -> /HEC_IO/A2
- U1 pad 33: /HEC_Memory/A3 -> /HEC_IO/A3
- U1 pad 34: /HEC_Memory/A4 -> /HEC_IO/A4
- U1 pad 35: /HEC_Memory/A5 -> /HEC_IO/A5
- U1 pad 36: /HEC_Memory/A6 -> /HEC_IO/A6
- U1 pad 37: /HEC_Memory/A7 -> /HEC_IO/A7
- U1 pad 38: /HEC_Memory/A8 -> /HEC_IO/A8
- U1 pad 39: /HEC_Memory/A9 -> /HEC_IO/A9
- U1 pad 4: /HEC_Memory/A14 -> /HEC_IO/A14
- U1 pad 40: /HEC_Memory/A10 -> /HEC_IO/A10
- U1 pad 5: /HEC_Memory/A15 -> /HEC_IO/A15
- U10 pad 14: VCC -> H
- U10 pad 7: GND -> L
- U11 pad 12: /MEC_Protection/~{WR} -> /HEC_CPU/~{WR}
- U11 pad 14: VCC -> H
- U11 pad 7: GND -> L
- U13 pad 1: /HEC_Memory/~{WR} -> /HEC_CPU/~{WR}
- U13 pad 10: GND -> L
- U13 pad 19: /HEC_Memory/PAGE_L -> /HEC_Memory/~{PAGE_L}
- U13 pad 20: VCC -> H
- U14 pad 1: /HEC_Memory/~{WR} -> /HEC_CPU/~{WR}
- U14 pad 10: GND -> L
- U14 pad 19: /HEC_Memory/PAGE_H -> /HEC_Memory/~{PAGE_H}
- U14 pad 20: VCC -> H
- U15 pad 1: /HEC_Memory/~{WR} -> /HEC_CPU/~{WR}
- U15 pad 10: /HEC_Memory/~{MREQ} -> /HEC_CPU/~{MREQ}
- U15 pad 13: /HEC_Memory/~{MREQ} -> /HEC_CPU/~{MREQ}
- U15 pad 14: VCC -> H
- U15 pad 4: /HEC_Memory/~{RD} -> /HEC_CPU/~{RD}
- U15 pad 7: GND -> L
- U16 pad 1: /HEC_Memory/~{WR} -> /HEC_CPU/~{WR}
- U16 pad 14: VCC -> H
- U16 pad 2: /HEC_Memory/PAGE_L -> /HEC_Memory/~{PAGE_L}
- U16 pad 4: /HEC_Memory/~{WR} -> /HEC_CPU/~{WR}
- U16 pad 5: /HEC_Memory/PAGE_H -> /HEC_Memory/~{PAGE_H}
- U16 pad 7: GND -> L
- U18 pad 1: /HEC_Memory/A0 -> /HEC_IO/A0
- U18 pad 16: VCC -> H
- U18 pad 2: /HEC_Memory/A1 -> /HEC_IO/A1
- U18 pad 3: /HEC_Memory/A2 -> /HEC_IO/A2
- U18 pad 4: /HEC_CPU/IO_CS0 -> /HEC_CPU/~{IO_CS0}
- U18 pad 5: /HEC_CPU/L -> L
- U18 pad 6: /HEC_Memory/A3 -> /HEC_IO/A3
- U18 pad 8: GND -> L
- U19 pad 1: /HEC_Memory/A0 -> /HEC_IO/D0
- U19 pad 14: VCC -> H
- U19 pad 2: /HEC_Memory/A1 -> /HEC_IO/D1
- U19 pad 3: /HEC_Memory/A2 -> /HEC_IO/D2
- U19 pad 4: /HEC_Memory/A6 -> /HEC_IO/D6
- U19 pad 5: /HEC_Memory/A7 -> /HEC_IO/D7
- U19 pad 7: GND -> L
- U2 pad 10: /HEC_Memory/A2 -> /HEC_IO/A2
- U2 pad 11: /HEC_Memory/A1 -> /HEC_IO/A1
- U2 pad 12: /HEC_Memory/A0 -> /HEC_IO/A0
- U2 pad 16: GND -> L
- U2 pad 32: VCC -> H
- U2 pad 5: /HEC_Memory/A7 -> /HEC_IO/A7
- U2 pad 6: /HEC_Memory/A6 -> /HEC_IO/A6
- U2 pad 7: /HEC_Memory/A5 -> /HEC_IO/A5
- U2 pad 8: /HEC_Memory/A4 -> /HEC_IO/A4
- U2 pad 9: /HEC_Memory/A3 -> /HEC_IO/A3
- U20 pad 10: GND -> L
- U20 pad 2: /HEC_Memory/A0 -> /HEC_IO/A0
- U20 pad 20: VCC -> H
- U20 pad 3: /HEC_Memory/A1 -> /HEC_IO/A1
- U20 pad 4: /HEC_Memory/A2 -> /HEC_IO/A2
- U20 pad 5: /HEC_Memory/A3 -> /HEC_IO/A3
- U20 pad 6: /HEC_Memory/A4 -> /HEC_IO/A4
- U20 pad 7: /HEC_Memory/A5 -> /HEC_IO/A5
- U20 pad 8: /HEC_Memory/A6 -> /HEC_IO/A6
- U20 pad 9: /HEC_Memory/A7 -> /HEC_IO/A7
- U21 pad 10: GND -> L
- U21 pad 2: /HEC_Memory/A8 -> /HEC_IO/A8
- U21 pad 20: VCC -> H
- U21 pad 3: /HEC_Memory/A9 -> /HEC_IO/A9
- U21 pad 4: /HEC_Memory/A10 -> /HEC_IO/A10
- U21 pad 5: /HEC_Memory/A11 -> /HEC_IO/A11
- U21 pad 6: /HEC_Memory/A12 -> /HEC_IO/A12
- U21 pad 7: /HEC_Memory/A13 -> /HEC_IO/A13
- U21 pad 8: /HEC_Memory/A14 -> /HEC_IO/A14
- U21 pad 9: /HEC_Memory/A15 -> /HEC_IO/A15
- U23 pad 11: /HEC_CPU/L -> L
- U23 pad 12: /HEC_CPU/L -> L
- U23 pad 14: VCC -> H
- U23 pad 7: GND -> L
- U24 pad 14: VCC -> H
- U24 pad 7: GND -> L
- U25 pad 10: GND -> L
- U25 pad 11: /HEC_Memory/A7 -> /HEC_IO/D7
- U25 pad 12: /HEC_Memory/A6 -> /HEC_IO/D6
- U25 pad 13: /HEC_Memory/A5 -> /HEC_IO/D5
- U25 pad 14: /HEC_Memory/A4 -> /HEC_IO/D4
- U25 pad 15: /HEC_Memory/A3 -> /HEC_IO/D3
- U25 pad 16: /HEC_Memory/A2 -> /HEC_IO/D2
- U25 pad 17: /HEC_Memory/A1 -> /HEC_IO/D1
- U25 pad 18: /HEC_Memory/A0 -> /HEC_IO/D0
- U25 pad 20: VCC -> H
- U26 pad 10: GND -> L
- U26 pad 11: /HEC_Memory/A7 -> /HEC_IO/D7
- U26 pad 12: /HEC_Memory/A6 -> /HEC_IO/D6
- U26 pad 13: /HEC_Memory/A5 -> /HEC_IO/D5
- U26 pad 14: /HEC_Memory/A4 -> /HEC_IO/D4
- U26 pad 15: /HEC_Memory/A3 -> /HEC_IO/D3
- U26 pad 16: /HEC_Memory/A2 -> /HEC_IO/D2
- U26 pad 17: /HEC_Memory/A1 -> /HEC_IO/D1
- U26 pad 18: /HEC_Memory/A0 -> /HEC_IO/D0
- U26 pad 2: /MEC_Protection/~{EXT_INT0} -> /HEC_IO/~{SENSE1}
- U26 pad 20: VCC -> H
- U26 pad 3: /MEC_Protection/~{EXT_INT1} -> /HEC_IO/~{SENSE2}
- U26 pad 4: /MEC_Protection/~{EXT_INT2} -> /HEC_IO/~{SENSE3}
- U26 pad 5: /MEC_Protection/~{EXT_INT3} -> /HEC_IO/~{SENSE4}
- U26 pad 6: /MEC_Protection/~{EXT_INT4} -> /HEC_IO/~{IRQ1}
- U26 pad 7: /MEC_Protection/~{EXT_INT5} -> /HEC_IO/~{IRQ2}
- U26 pad 8: /MEC_Protection/~{EXT_INT6} -> /HEC_IO/~{IRQ3}
- U26 pad 9: /MEC_Protection/~{EXT_INT7} -> /HEC_IO/~{IRQ4}
- U27 pad 14: VCC -> H
- U27 pad 7: GND -> L
- U28 pad 14: VCC -> H
- U28 pad 7: GND -> L
- U29 pad 14: VCC -> H
- U29 pad 7: GND -> L
- U3 pad 10: /HEC_Memory/A2 -> /HEC_IO/A2
- U3 pad 11: /HEC_Memory/A1 -> /HEC_IO/A1
- U3 pad 12: /HEC_Memory/A0 -> /HEC_IO/A0
- U3 pad 16: GND -> L
- U3 pad 32: VCC -> H
- U3 pad 5: /HEC_Memory/A7 -> /HEC_IO/A7
- U3 pad 6: /HEC_Memory/A6 -> /HEC_IO/A6
- U3 pad 7: /HEC_Memory/A5 -> /HEC_IO/A5
- U3 pad 8: /HEC_Memory/A4 -> /HEC_IO/A4
- U3 pad 9: /HEC_Memory/A3 -> /HEC_IO/A3
- U4 pad 1: /HEC_Memory/A13 -> /HEC_IO/A13
- U4 pad 14: GND -> L
- U4 pad 2: /HEC_Memory/A14 -> /HEC_IO/A14
- U4 pad 21: /HEC_Memory/A8 -> /HEC_IO/A8
- U4 pad 23: /HEC_Memory/A9 -> /HEC_IO/A9
- U4 pad 24: /HEC_Memory/A10 -> /HEC_IO/A10
- U4 pad 25: /HEC_Memory/A11 -> /HEC_IO/A11
- U4 pad 26: /HEC_Memory/A12 -> /HEC_IO/A12
- U4 pad 28: VCC -> H
- U4 pad 3: /HEC_Memory/A15 -> /HEC_IO/A15
- U5 pad 1: /HEC_Memory/A13 -> /HEC_IO/A13
- U5 pad 14: GND -> L
- U5 pad 2: /HEC_Memory/A14 -> /HEC_IO/A14
- U5 pad 21: /HEC_Memory/A8 -> /HEC_IO/A8
- U5 pad 23: /HEC_Memory/A9 -> /HEC_IO/A9
- U5 pad 24: /HEC_Memory/A10 -> /HEC_IO/A10
- U5 pad 25: /HEC_Memory/A11 -> /HEC_IO/A11
- U5 pad 26: /HEC_Memory/A12 -> /HEC_IO/A12
- U5 pad 28: VCC -> H
- U5 pad 3: /HEC_Memory/A15 -> /HEC_IO/A15
- U7 pad 1: /HEC_Memory/A14 -> /HEC_IO/A14
- U7 pad 10: /HEC_Memory/A0 -> /HEC_IO/A0
- U7 pad 14: unconnected-(U7-GND-Pad14) -> L
- U7 pad 2: /HEC_Memory/A12 -> /HEC_IO/A12
- U7 pad 20: /HEC_Memory/A15 -> /HEC_IO/A15
- U7 pad 21: /HEC_Memory/A10 -> /HEC_IO/A10
- U7 pad 23: /HEC_Memory/A11 -> /HEC_IO/A11
- U7 pad 24: /HEC_Memory/A9 -> /HEC_IO/A9
- U7 pad 25: /HEC_Memory/A8 -> /HEC_IO/A8
- U7 pad 26: /HEC_Memory/A13 -> /HEC_IO/A13
- U7 pad 27: /HEC_CPU/H -> H
- U7 pad 28: unconnected-(U7-VCC-Pad28) -> H
- U7 pad 3: /HEC_Memory/A7 -> /HEC_IO/A7
- U7 pad 4: /HEC_Memory/A6 -> /HEC_IO/A6
- U7 pad 5: /HEC_Memory/A5 -> /HEC_IO/A5
- U7 pad 6: /HEC_Memory/A4 -> /HEC_IO/A4
- U7 pad 7: /HEC_Memory/A3 -> /HEC_IO/A3
- U7 pad 8: /HEC_Memory/A2 -> /HEC_IO/A2
- U7 pad 9: /HEC_Memory/A1 -> /HEC_IO/A1
- U8 pad 1: /MEC_Protection/A0 -> /HEC_IO/A0
- U8 pad 14: /MEC_Protection/PAGE_H -> /HEC_Memory/~{PAGE_H}
- U8 pad 15: /MEC_Protection/PAGE_L -> /HEC_Memory/~{PAGE_L}
- U8 pad 16: VCC -> H
- U8 pad 2: /MEC_Protection/A1 -> /HEC_IO/A1
- U8 pad 3: /MEC_Protection/A2 -> /HEC_IO/A2
- U8 pad 5: /MEC_Protection/A3 -> /HEC_IO/A3
- U8 pad 8: GND -> L
- U8 pad 9: /MEC_Protection/~{RAMEN} -> /HEC_CPU/~{RAMEN}
- U9 pad 10: GND -> L
- U9 pad 20: VCC -> H
